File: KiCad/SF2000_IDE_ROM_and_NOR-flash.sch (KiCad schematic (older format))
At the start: 6 parts, among them J20 Conn_02x11_Odd_Even, U14 SST39LF040, U15 SST39LF802C, U16 74AHCT3G14

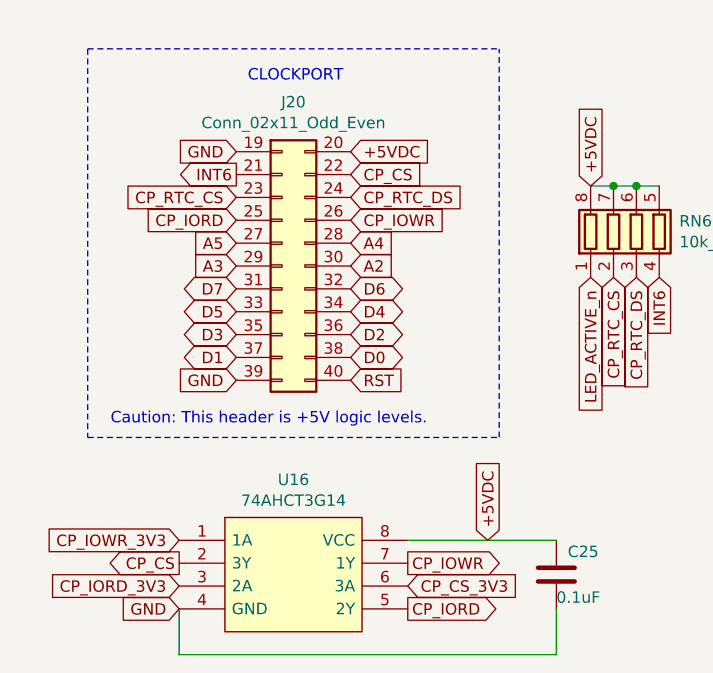
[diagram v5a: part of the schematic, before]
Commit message: Fix of SD-card control signals and routing
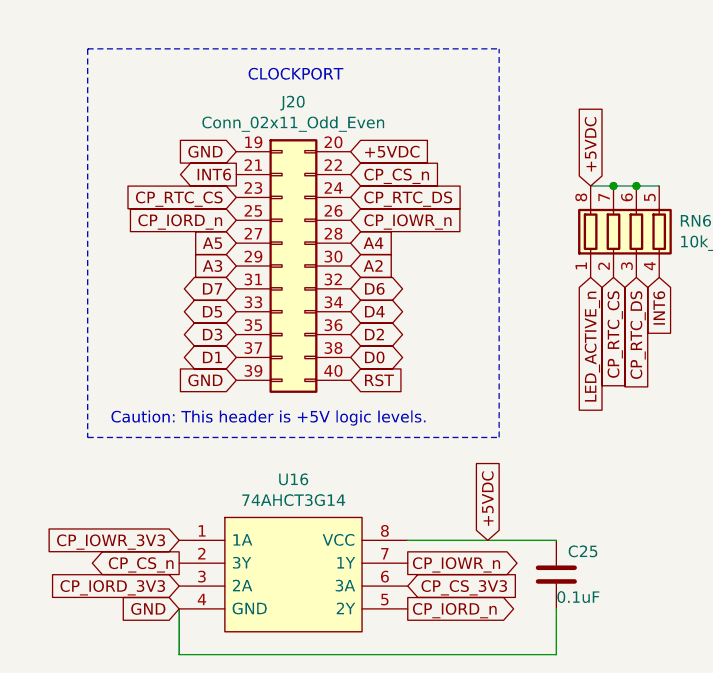
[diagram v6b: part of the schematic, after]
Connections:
- net CP_CS renamed CP_CS_n
- net CP_IORD renamed CP_IORD_n
- net CP_IOWR renamed CP_IOWR_n
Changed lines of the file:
@@
 CP_RTC_DS
 Text GLabel 2450 2950 0    50   Input ~ 0
-CP_IORD
+CP_IORD_n
 Text GLabel 2950 2950 2    50   Input ~ 0
-CP_IOWR
+CP_IOWR_n
 Text GLabel 2950 2750 2    50   Input ~ 0
-CP_CS
+CP_CS_n
 Text GLabel 4000 2800 1    50   Input ~ 0
 +5VDC
@@
 GND
 Text GLabel 2200 4450 0    50   Output ~ 0
-CP_CS
+CP_CS_n
 Text GLabel 3200 4450 2    50   Output ~ 0
-CP_IOWR
+CP_IOWR_n
 Text GLabel 3200 4650 2    50   Output ~ 0
-CP_IORD
+CP_IORD_n
 Text GLabel 2450 2750 0    50   Output ~ 0
 INT6

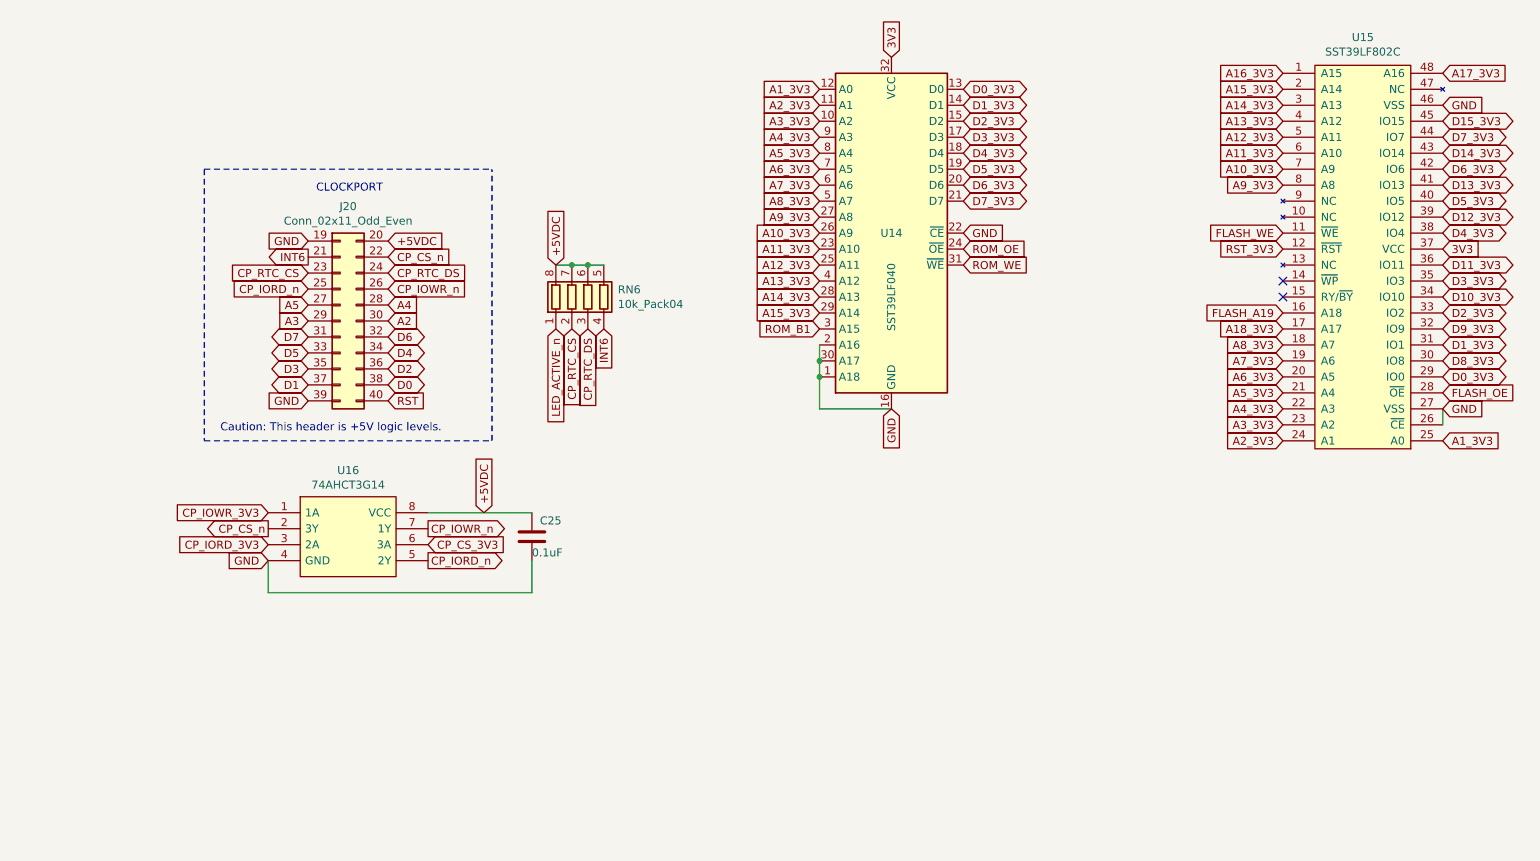
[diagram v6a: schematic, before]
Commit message: Replace 74AHCT3G14 with a hex inverter 74AHCT14PW and also simplify and drive the LED circuit from this latter IC.
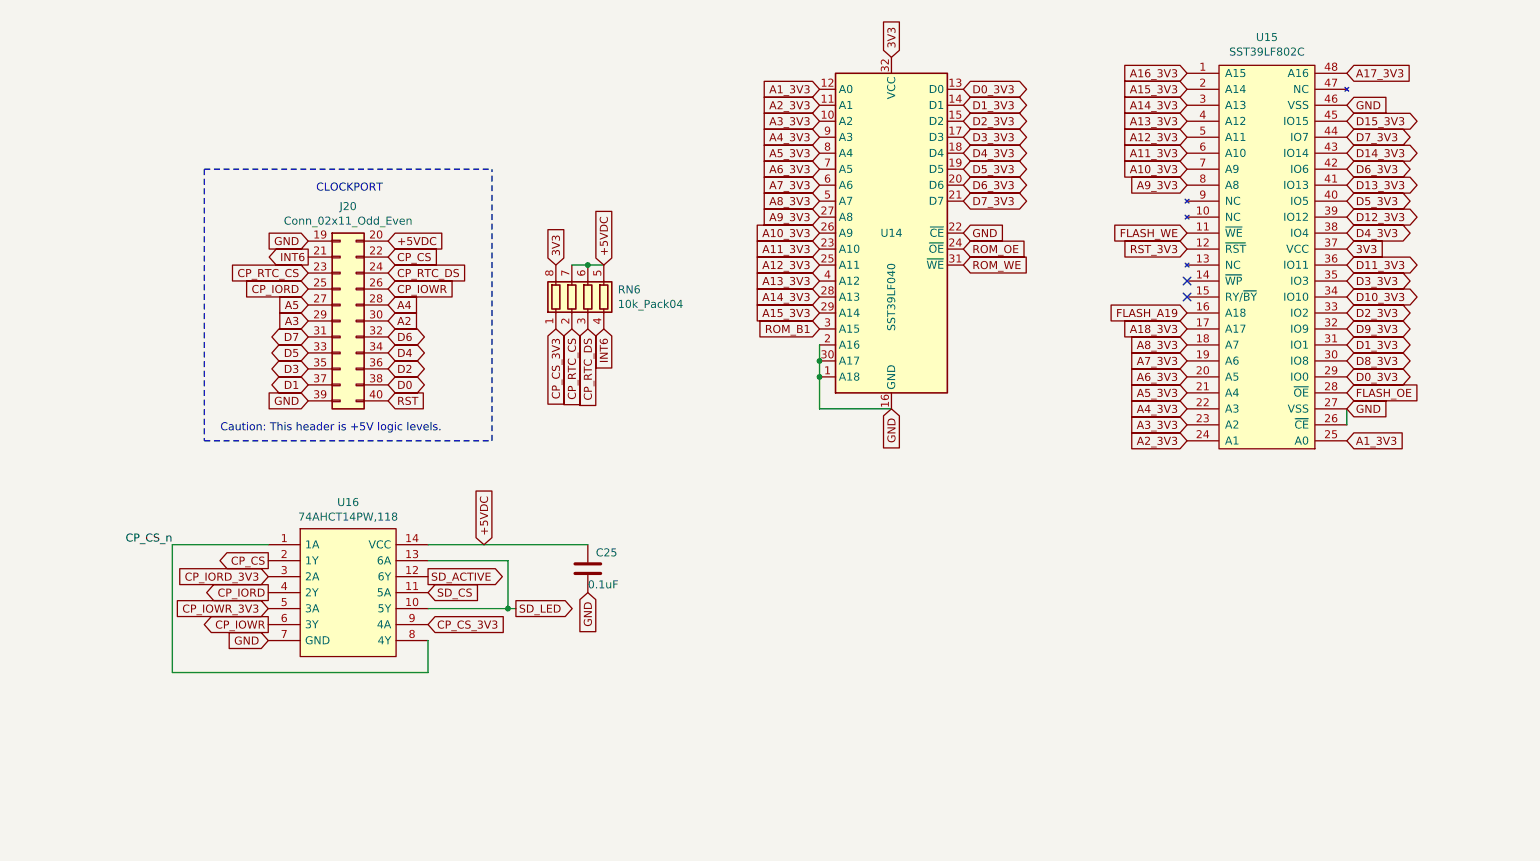
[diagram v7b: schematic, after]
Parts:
- removed U16: 74AHCT3G14, Package_SO:TSSOP-8_3x3mm_P0.65mm, symbol SF2000:74AHCT3G14
- added U16: 74AHCT14PW,118, Package_SO:TSSOP-14_4.4x5mm_P0.65mm, symbol SF2000:74AHCT14PW,118
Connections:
- net LED_ACTIVE_n is gone; now on net CP_CS_3V3: RN6.1 (R1.1)
- net +5VDC: now also U16.14 (VCC); no longer RN6.8 (R1.2)
- net 3V3: now also RN6.8 (R1.2)
- net CP_CS_3V3: now also U16.9 (4A)
- net CP_CS_n: now also U16.1 (1A), U16.8 (4Y); no longer J20.22 (Pin_22)
- net CP_IORD_3V3: now also U16.3 (2A)
- net CP_IOWR_3V3: now also U16.5 (3A)
- net GND: now also U16.7 (GND)
- net CP_IORD_n renamed CP_IORD
- net CP_IORD: now also U16.4 (2Y)
- net CP_IOWR_n renamed CP_IOWR
- net CP_IOWR: now also U16.6 (3Y)
- new net CP_CS: J20.22 (Pin_22), U16.2 (1Y)
- new net SD_ACTIVE: U16.12 (6Y)
- new net SD_CS: U16.11 (5A)
- new net SD_LED: U16.10 (5Y), U16.13 (6A)
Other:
- moved on the sheet: C25, U15
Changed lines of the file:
@@
 L SF2000:SST39LF802C-55-4C-EKE U15
 U 1 1 627FF0EA
-P 9050 2700
-F 0 "U15" H 9050 4025 50  0000 C CNN
-F 1 "SST39LF802C" H 9050 3934 50  0000 C CNN
-F 2 "Package_SO:TSOP-I-48_18.4x12mm_P0.5mm" H 9050 3250 50  0001 C CNN
-F 3 "https://www.mouser.se/datasheet/2/268/25041A-47515.pdf" H 9050 3250 50  0001 C CNN
-	1    9050 2700
-	1    0    0    -1
-$EndComp
-Text GLabel 8550 3600 0    50   Input ~ 0
+P 8450 2700
+F 0 "U15" H 8450 4025 50  0000 C CNN
+F 1 "SST39LF802C" H 8450 3934 50  0000 C CNN
+F 2 "Package_SO:TSOP-I-48_18.4x12mm_P0.5mm" H 8450 3250 50  0001 C CNN
+F 3 "https://www.mouser.se/datasheet/2/268/25041A-47515.pdf" H 8450 3250 50  0001 C CNN
+	1    8450 2700
+	1    0    0    -1
+$EndComp
+Text GLabel 7950 3600 0    50   Input ~ 0
 A5_3V3
-Text GLabel 8550 3500 0    50   Input ~ 0
+Text GLabel 7950 3500 0    50   Input ~ 0
 A6_3V3
-Text GLabel 8550 3700 0    50   Input ~ 0
+Text GLabel 7950 3700 0    50   Input ~ 0
 A4_3V3
-Text GLabel 8550 3800 0    50   Input ~ 0
+Text GLabel 7950 3800 0    50   Input ~ 0
 A3_3V3
-Text GLabel 8550 3400 0    50   Input ~ 0
+Text GLabel 7950 3400 0    50   Input ~ 0
 A7_3V3
-Text GLabel 8550 3300 0    50   Input ~ 0
+Text GLabel 7950 3300 0    50   Input ~ 0
 A8_3V3
-Text GLabel 8550 3900 0    50   Input ~ 0
+Text GLabel 7950 3900 0    50   Input ~ 0
 A2_3V3
-Text GLabel 9550 3900 2    50   Input ~ 0
+Text GLabel 8950 3900 2    50   Input ~ 0
 A1_3V3
-Text GLabel 8550 2100 0    50   Input ~ 0
+Text GLabel 7950 2100 0    50   Input ~ 0
 A11_3V3
-Text GLabel 8550 2300 0    50   Input ~ 0
+Text GLabel 7950 2300 0    50   Input ~ 0
 A9_3V3
-Text GLabel 8550 2200 0    50   Input ~ 0
+Text GLabel 7950 2200 0    50   Input ~ 0
 A10_3V3
-Text GLabel 8550 2000 0    50   Input ~ 0
+Text GLabel 7950 2000 0    50   Input ~ 0
 A12_3V3
-Text GLabel 8550 1900 0    50   Input ~ 0
+Text GLabel 7950 1900 0    50   Input ~ 0
 A13_3V3
-Text GLabel 8550 1800 0    50   Input ~ 0
+Text GLabel 7950 1800 0    50   Input ~ 0
 A14_3V3
-Text GLabel 8550 1700 0    50   Input ~ 0
+Text GLabel 7950 1700 0    50   Input ~ 0
 A15_3V3
-Text GLabel 8550 1600 0    50   Input ~ 0
+Text GLabel 7950 1600 0    50   Input ~ 0
 A16_3V3
-Text GLabel 9550 1600 2    50   Input ~ 0
+Text GLabel 8950 1600 2    50   Input ~ 0
 A17_3V3
-Text GLabel 8550 3200 0    50   Input ~ 0
+Text GLabel 7950 3200 0    50   Input ~ 0
 A18_3V3
-Text GLabel 8550 3100 0    50   Input ~ 0
+Text GLabel 7950 3100 0    50   Input ~ 0
 FLASH_A19
-Text GLabel 9550 1800 2    50   Input ~ 0
-GND
-Text GLabel 9550 3700 2    50   Input ~ 0
-GND
-Text GLabel 9550 2700 2    50   Input ~ 0
+Text GLabel 8950 1800 2    50   Input ~ 0
+GND
+Text GLabel 8950 3700 2    50   Input ~ 0
+GND
+Text GLabel 8950 2700 2    50   Input ~ 0
 3V3
 Text GLabel 5650 2100 0    50   Input ~ 0
@@
 Text GLabel 5650 3200 0    50   Input ~ 0
 ROM_B1
-Text GLabel 9550 3500 2    50   BiDi ~ 0
+Text GLabel 8950 3500 2    50   BiDi ~ 0
 D0_3V3
-Text GLabel 9550 3300 2    50   BiDi ~ 0
+Text GLabel 8950 3300 2    50   BiDi ~ 0
 D1_3V3
-Text GLabel 9550 3100 2    50   BiDi ~ 0
+Text GLabel 8950 3100 2    50   BiDi ~ 0
 D2_3V3
-Text GLabel 9550 2900 2    50   BiDi ~ 0
+Text GLabel 8950 2900 2    50   BiDi ~ 0
 D3_3V3
-Text GLabel 9550 2600 2    50   BiDi ~ 0
+Text GLabel 8950 2600 2    50   BiDi ~ 0
 D4_3V3
-Text GLabel 9550 2400 2    50   BiDi ~ 0
+Text GLabel 8950 2400 2    50   BiDi ~ 0
 D5_3V3
-Text GLabel 9550 2200 2    50   BiDi ~ 0
+Text GLabel 8950 2200 2    50   BiDi ~ 0
 D6_3V3
-Text GLabel 9550 2000 2    50   BiDi ~ 0
+Text GLabel 8950 2000 2    50   BiDi ~ 0
 D7_3V3
-Text GLabel 9550 3400 2    50   BiDi ~ 0
+Text GLabel 8950 3400 2    50   BiDi ~ 0
 D8_3V3
-Text GLabel 9550 3200 2    50   BiDi ~ 0
+Text GLabel 8950 3200 2    50   BiDi ~ 0
 D9_3V3
-Text GLabel 9550 3000 2    50   BiDi ~ 0
+Text GLabel 8950 3000 2    50   BiDi ~ 0
 D10_3V3
-Text GLabel 9550 2800 2    50   BiDi ~ 0
+Text GLabel 8950 2800 2    50   BiDi ~ 0
 D11_3V3
-Text GLabel 9550 2500 2    50   BiDi ~ 0
+Text GLabel 8950 2500 2    50   BiDi ~ 0
 D12_3V3
-Text GLabel 9550 2300 2    50   BiDi ~ 0
+Text GLabel 8950 2300 2    50   BiDi ~ 0
 D13_3V3
-Text GLabel 9550 2100 2    50   BiDi ~ 0
+Text GLabel 8950 2100 2    50   BiDi ~ 0
 D14_3V3
-Text GLabel 9550 1900 2    50   BiDi ~ 0
+Text GLabel 8950 1900 2    50   BiDi ~ 0
 D15_3V3
 Wire Wire Line
-	9550 3800 9550 3700
-Text GLabel 9550 3600 2    50   Input ~ 0
+	8950 3800 8950 3700
+Text GLabel 8950 3600 2    50   Input ~ 0
 FLASH_OE
-Text GLabel 8550 2600 0    50   Input ~ 0
+Text GLabel 7950 2600 0    50   Input ~ 0
 FLASH_WE
 Text GLabel 6550 2700 2    50   Input ~ 0
@@
 Text GLabel 6550 2400 2    50   BiDi ~ 0
 D7_3V3
-Text GLabel 2200 4350 0    50   Input ~ 0
+Text GLabel 2200 4950 0    50   Input ~ 0
 CP_IOWR_3V3
-Text GLabel 2200 4550 0    50   Input ~ 0
+Text GLabel 2200 4750 0    50   Input ~ 0
 CP_IORD_3V3
-Text GLabel 3200 4550 2    50   Input ~ 0
-CP_CS_3V3
 Wire Wire Line
 	6100 3700 5650 3700
@@
 Text GLabel 6100 1500 1    50   Input ~ 0
 3V3
-NoConn ~ 8550 3000
-NoConn ~ 8550 2900
-Text GLabel 8550 2700 0    50   Input ~ 0
+NoConn ~ 7950 3000
+NoConn ~ 7950 2900
+Text GLabel 7950 2700 0    50   Input ~ 0
 RST_3V3
 $Comp
@@
 CP_RTC_DS
 Text GLabel 2450 2950 0    50   Input ~ 0
-CP_IORD_n
+CP_IORD
 Text GLabel 2950 2950 2    50   Input ~ 0
-CP_IOWR_n
+CP_IOWR
 Text GLabel 2950 2750 2    50   Input ~ 0
-CP_CS_n
-Text GLabel 4000 2800 1    50   Input ~ 0
+CP_CS
+Text GLabel 4300 2800 1    50   Input ~ 0
 +5VDC
 Text GLabel 4300 3200 3    50   Input ~ 0
@@
 $EndComp
 Wire Wire Line
-	4000 2800 4100 2800
-Wire Wire Line
 	4100 2800 4200 2800
-Connection ~ 4100 2800
 Connection ~ 4200 2800
 Wire Wire Line
 	4200 2800 4300 2800
-$Comp
-L SF2000:74AHCT3G14 U16
-U 1 1 681A2173
-P 2700 4500
-F 0 "U16" H 2700 4915 50  0000 C CNN
-F 1 "74AHCT3G14" H 2700 4824 50  0000 C CNN
-F 2 "Package_SO:TSSOP-8_3x3mm_P0.65mm" H 3050 4750 50  0001 L CNN
-F 3 "https://assets.nexperia.com/documents/data-sheet/74AHC_AHCT3G14.pdf" H 3050 4650 50  0001 L CNN
-	1    2700 4500
-	1    0    0    -1
-$EndComp
-Text GLabel 3550 4350 1    50   Input ~ 0
+Text GLabel 3550 4550 1    50   Input ~ 0
 +5VDC
-Text GLabel 2200 4650 0    50   Input ~ 0
-GND
-Text GLabel 2200 4450 0    50   Output ~ 0
-CP_CS_n
-Text GLabel 3200 4450 2    50   Output ~ 0
-CP_IOWR_n
-Text GLabel 3200 4650 2    50   Output ~ 0
-CP_IORD_n
+Text GLabel 4200 4850 3    50   Input ~ 0
+GND
+Text GLabel 2200 5050 0    50   Output ~ 0
+CP_IOWR
 Text GLabel 2450 2750 0    50   Output ~ 0
 INT6
@@
 Wire Notes Line
 	1800 2200 3600 2200
-Text GLabel 4000 3200 3    50   Input ~ 0
-LED_ACTIVE_n
+Text GLabel 3750 4950 2    50   Output ~ 0
+SD_LED
 $Comp
 L Device:C C?
 U 1 1 683D3421
-P 3850 4500
+P 4200 4700
 AR Path="/683D3421" Ref="C?"  Part="1"
 AR Path="/620D263D/683D3421" Ref="C?"  Part="1"
 AR Path="/627A6500/683D3421" Ref="C25"  Part="1"
-F 0 "C25" H 3900 4600 50  0000 L CNN
-F 1 "0.1uF" H 3850 4400 50  0000 L CNN
-F 2 "Capacitor_SMD:C_0805_2012Metric_Pad1.18x1.45mm_HandSolder" H 3888 4350 50  0001 C CNN
-F 3 "~" H 3850 4500 50  0001 C CNN
-	1    3850 4500
-	1    0    0    -1
-$EndComp
-Wire Wire Line
-	3850 4350 3200 4350
-Wire Wire Line
-	3850 4650 3850 4850
-Wire Wire Line
-	3850 4850 2200 4850
-Wire Wire Line
-	2200 4850 2200 4650
+F 0 "C25" H 4250 4800 50  0000 L CNN
+F 1 "0.1uF" H 4200 4600 50  0000 L CNN
+F 2 "Capacitor_SMD:C_0805_2012Metric_Pad1.18x1.45mm_HandSolder" H 4238 4550 50  0001 C CNN
+F 3 "~" H 4200 4700 50  0001 C CNN
+	1    4200 4700
+	1    0    0    -1
+$EndComp
 Wire Wire Line
 	5650 3300 5650 3400
 Connection ~ 5650 3400
+$Comp
+L SF2000:74AHCT14PW,118 U16
+U 1 1 6802794C
+P 2700 4850
+F 0 "U16" H 2700 5415 50  0000 C CNN
+F 1 "74AHCT14PW,118" H 2700 5324 50  0000 C CNN
+F 2 "Package_SO:TSSOP-14_4.4x5mm_P0.65mm" H 3050 5250 50  0001 L CNN
+F 3 "https://assets.nexperia.com/documents/data-sheet/74AHC_AHCT14.pdf" H 3050 5150 50  0001 L CNN
+	1    2700 4850
+	1    0    0    -1
+$EndComp
+Text GLabel 3200 5050 2    50   Input ~ 0
+CP_CS_3V3
+Text GLabel 2200 5150 0    50   Input ~ 0
+GND
+Text GLabel 2200 4650 0    50   Output ~ 0
+CP_CS
+Text GLabel 2200 4850 0    50   Output ~ 0
+CP_IORD
+Text Label 1600 4550 2    50   ~ 0
+CP_CS_n
+Wire Wire Line
+	3200 5150 3200 5350
+Wire Wire Line
+	3200 5350 1600 5350
+Wire Wire Line
+	1600 5350 1600 4550
+Wire Wire Line
+	1600 4550 2200 4550
+Text GLabel 4000 2800 1    50   Input ~ 0
+3V3
+Text GLabel 4000 3200 3    50   Input ~ 0
+CP_CS_3V3
+Text GLabel 3200 4850 2    50   Input ~ 0
+SD_CS
+Text GLabel 3200 4750 2    50   Output ~ 0
+SD_ACTIVE
+Wire Wire Line
+	3200 4550 4200 4550
+Wire Wire Line
+	3200 4950 3700 4950
+Wire Wire Line
+	3700 4950 3700 4650
+Wire Wire Line
+	3700 4650 3200 4650
+Connection ~ 3700 4950
+Wire Wire Line
+	3700 4950 3750 4950
 $EndSCHEMATC

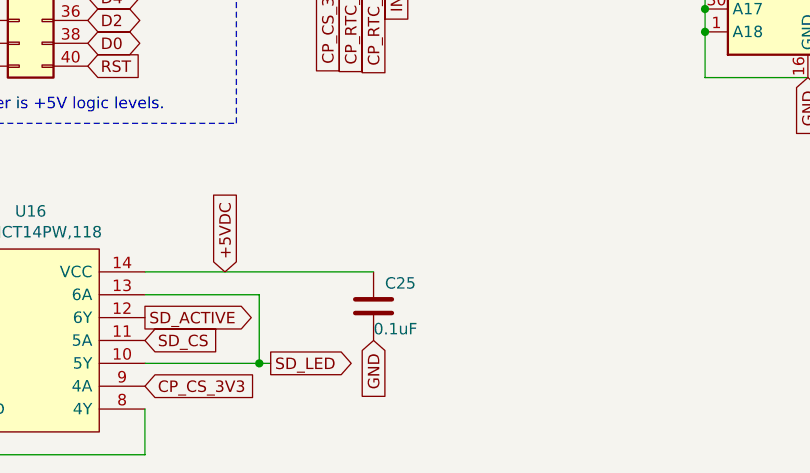
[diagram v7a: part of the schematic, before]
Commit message: Fixed references to capacitors in ascending order by size and value
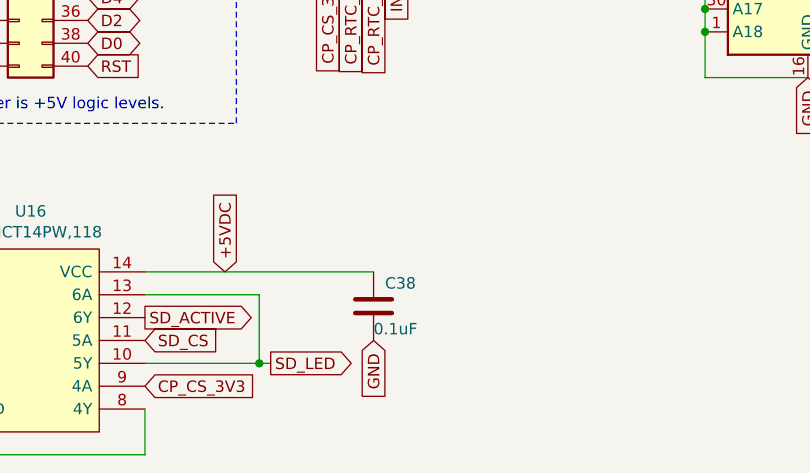
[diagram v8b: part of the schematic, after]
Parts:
- renumbered C25 to C38
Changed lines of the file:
@@
 AR Path="/683D3421" Ref="C?"  Part="1"
 AR Path="/620D263D/683D3421" Ref="C?"  Part="1"
-AR Path="/627A6500/683D3421" Ref="C25"  Part="1"
-F 0 "C25" H 4250 4800 50  0000 L CNN
+AR Path="/627A6500/683D3421" Ref="C38"  Part="1"
+F 0 "C38" H 4250 4800 50  0000 L CNN
 F 1 "0.1uF" H 4200 4600 50  0000 L CNN
 F 2 "Capacitor_SMD:C_0805_2012Metric_Pad1.18x1.45mm_HandSolder" H 4238 4550 50  0001 C CNN
